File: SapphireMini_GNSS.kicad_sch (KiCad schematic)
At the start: 7 parts, among them J401 Conn_01x01_Male, J402 Conn_01x04_Male, U402 SAM-M8Q-0-10

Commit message: Start of layout
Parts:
- added R402, R403: 0, Resistor_SMD:R_0603_1608Metric, symbol Device:R_Small_US
- C401: footprint Capacitor_SMD:C_0603_1608Metric -> Capacitor_SMD:C_0402_1005Metric
- R401: MPN (none) -> EXB-2HV470JV
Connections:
- net SAM_SCL: now also R402.2; no longer U402.12 (SCL)
- net SAM_SDA: now also R403.2; no longer U402.9 (SDA)
- new net: R402.1, U402.12 (SCL)
- new net: R403.1, U402.9 (SDA)
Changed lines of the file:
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@@
     (comment 2 "Markup copy w/ errors!")
   )
-  (junction (at 64.77 46.99) (diameter 0) (color 0 0 0 0)
-  )
   (junction (at 95.25 90.17) (diameter 0) (color 0 0 0 0)
   )
   (junction (at 95.25 46.99) (diameter 0) (color 0 0 0 0)
   )
-  (junction (at 134.62 92.71) (diameter 0) (color 0 0 0 0)
-  )
   (junction (at 95.25 95.25) (diameter 0) (color 0 0 0 0)
   )
@@
     (stroke (width 0) (type default) (color 0 0 0 0))
   )
+  (wire (pts (xy 115.57 107.95) (xy 135.89 107.95))
+    (stroke (width 0) (type default) (color 0 0 0 0))
+  )
   (wire (pts (xy 110.49 55.88) (xy 111.76 54.61))
     (stroke (width 0) (type default) (color 0 0 0 0))
@@
     (stroke (width 0) (type default) (color 0 0 0 0))
   )
-  (wire (pts (xy 95.25 46.99) (xy 64.77 46.99))
+  (wire (pts (xy 55.88 46.99) (xy 95.25 46.99))
+    (stroke (width 0) (type default) (color 0 0 0 0))
+  )
+  (wire (pts (xy 115.57 105.41) (xy 135.89 105.41))
     (stroke (width 0) (type default) (color 0 0 0 0))
   )
@@
     (stroke (width 0) (type default) (color 0 0 0 0))
   )
-  (wire (pts (xy 115.57 105.41) (xy 135.89 105.41))
-    (stroke (width 0) (type default) (color 0 0 0 0))
-  )
   (wire (pts (xy 176.53 100.33) (xy 187.96 100.33))
     (stroke (width 0) (type default) (color 0 0 0 0))
@@
     (stroke (width 0) (type default) (color 0 0 0 0))
   )
-  (wire (pts (xy 115.57 92.71) (xy 134.62 92.71))
+  (wire (pts (xy 115.57 92.71) (xy 135.89 92.71))
     (stroke (width 0) (type default) (color 0 0 0 0))
   )
@@
     (stroke (width 0) (type default) (color 0 0 0 0))
   )
-  (wire (pts (xy 134.62 92.71) (xy 135.89 92.71))
-    (stroke (width 0) (type default) (color 0 0 0 0))
-  )
   (wire (pts (xy 40.64 85.09) (xy 52.07 85.09))
     (stroke (width 0) (type default) (color 0 0 0 0))
@@
     (stroke (width 0) (type default) (color 0 0 0 0))
   )
-  (wire (pts (xy 64.77 46.99) (xy 55.88 46.99))
-    (stroke (width 0) (type default) (color 0 0 0 0))
-  )
   (wire (pts (xy 115.57 100.33) (xy 135.89 100.33))
     (stroke (width 0) (type default) (color 0 0 0 0))
   )
+  (wire (pts (xy 182.88 105.41) (xy 194.31 105.41))
+    (stroke (width 0) (type default) (color 0 0 0 0))
+  )
   (wire (pts (xy 95.25 46.99) (xy 95.25 90.17))
     (stroke (width 0) (type default) (color 0 0 0 0))
@@
     (stroke (width 0) (type default) (color 0 0 0 0))
   )
-  (wire (pts (xy 115.57 107.95) (xy 135.89 107.95))
-    (stroke (width 0) (type default) (color 0 0 0 0))
-  )
   (wire (pts (xy 130.81 124.46) (xy 130.81 116.84))
     (stroke (width 0) (type default) (color 0 0 0 0))
@@
     (stroke (width 0) (type default) (color 0 0 0 0))
   )
-  (wire (pts (xy 176.53 105.41) (xy 187.96 105.41))
+  (wire (pts (xy 176.53 105.41) (xy 177.8 105.41))
     (stroke (width 0) (type default) (color 0 0 0 0))
   )
@@
     (stroke (width 0) (type default) (color 0 0 0 0))
   )
-  (wire (pts (xy 176.53 107.95) (xy 187.96 107.95))
+  (wire (pts (xy 182.88 107.95) (xy 194.31 107.95))
+    (stroke (width 0) (type default) (color 0 0 0 0))
+  )
+  (wire (pts (xy 176.53 107.95) (xy 177.8 107.95))
     (stroke (width 0) (type default) (color 0 0 0 0))
   )
@@
     (effects (font (size 1.27 1.27)) (justify left bottom))
   )
-  (label "SAM_SDA" (at 177.8 107.95 0)
-    (effects (font (size 1.27 1.27)) (justify left bottom))
-  )
-  (label "V_BCKP" (at 120.65 92.71 0)
+  (label "SAM_SDA" (at 185.42 107.95 0)
     (effects (font (size 1.27 1.27)) (justify left bottom))
   )
@@
     (effects (font (size 1.27 1.27)) (justify left bottom))
   )
-  (label "SAM_SCL" (at 177.8 105.41 0)
+  (label "SAM_SCL" (at 185.42 105.41 0)
     (effects (font (size 1.27 1.27)) (justify left bottom))
   )
@@
   )
   (label "SAM_SCL" (at 68.58 95.25 0)
+    (effects (font (size 1.27 1.27)) (justify left bottom))
+  )
+  (label "V_BCKP" (at 124.46 92.71 0)
     (effects (font (size 1.27 1.27)) (justify left bottom))
   )
@@
       (effects (font (size 1.27 1.27)) (justify left))
     )
-    (property "Footprint" "Capacitor_SMD:C_0603_1608Metric" (id 2) (at 95.25 101.6 0)
+    (property "Footprint" "Capacitor_SMD:C_0402_1005Metric" (id 2) (at 95.25 101.6 0)
       (effects (font (size 1.27 1.27)) hide)
     )
@@
     (pin "1")
   )
-  (symbol (lib_id "power:PWR_FLAG") (at 64.77 46.99 0) (unit 1)
-    (in_bom yes) (on_board yes) (fields_autoplaced)
-    (property "Reference" "#FLG0401" (id 0) (at 64.77 45.085 0)
-      (effects (font (size 1.27 1.27)) hide)
-    )
-    (property "Value" "PWR_FLAG" (id 1) (at 64.77 43.4142 0))
-    (property "Footprint" "" (id 2) (at 64.77 46.99 0)
-      (effects (font (size 1.27 1.27)) hide)
-    )
-    (property "Datasheet" "~" (id 3) (at 64.77 46.99 0)
-      (effects (font (size 1.27 1.27)) hide)
-    )
-    (pin "1")
+  (symbol (lib_id "Device:R_Small_US") (at 180.34 105.41 90) (unit 1)
+    (in_bom yes) (on_board yes)
+    (property "Reference" "R402" (id 0) (at 177.8 102.87 90)
+      (effects (font (size 1.27 1.27)) (justify right))
+    )
+    (property "Value" "0" (id 1) (at 180.34 102.87 90)
+      (effects (font (size 1.27 1.27)) (justify right))
+    )
+    (property "Footprint" "Resistor_SMD:R_0603_1608Metric" (id 2) (at 180.34 105.41 0)
+      (effects (font (size 1.27 1.27)) hide)
+    )
+    (property "Datasheet" "~" (id 3) (at 180.34 105.41 0)
+      (effects (font (size 1.27 1.27)) hide)
+    )
+    (property "MPN" "RMCF0603ZT0R00" (id 4) (at 180.34 105.41 0)
+      (effects (font (size 1.27 1.27)) hide)
+    )
+    (property "Manufacturer" "Vishay" (id 5) (at 180.34 105.41 0)
+      (effects (font (size 1.27 1.27)) hide)
+    )
+    (property "DPN" "WSLJ-.1CT-ND" (id 6) (at 180.34 105.41 0)
+      (effects (font (size 1.27 1.27)) hide)
+    )
+    (property "Populate" "1" (id 7) (at 180.34 105.41 0)
+      (effects (font (size 1.27 1.27)) hide)
+    )
+    (property "Description" "0 Ohms Jumper 0.1W, 1/10W Chip Resistor 0603 (1608 Metric) Automotive AEC-Q200 Thick Film" (id 8) (at 180.34 105.41 0)
+      (effects (font (size 1.27 1.27)) hide)
+    )
+    (property "Digi-Key_PN" "WSLJ-.1CT-ND" (id 9) (at 180.34 105.41 0)
+      (effects (font (size 1.27 1.27)) hide)
+    )
+    (property "Distributor" "Digikey" (id 10) (at 180.34 105.41 0)
+      (effects (font (size 1.27 1.27)) hide)
+    )
+    (pin "1")
+    (pin "2")
   )
   (symbol (lib_id "Device:FerriteBead") (at 46.99 105.41 90) (unit 1)
@@
     (pin "4")
   )
+  (symbol (lib_id "Device:R_Small_US") (at 180.34 107.95 90) (unit 1)
+    (in_bom yes) (on_board yes)
+    (property "Reference" "R403" (id 0) (at 177.8 110.49 90)
+      (effects (font (size 1.27 1.27)) (justify right))
+    )
+    (property "Value" "0" (id 1) (at 180.34 110.49 90)
+      (effects (font (size 1.27 1.27)) (justify right))
+    )
+    (property "Footprint" "Resistor_SMD:R_0603_1608Metric" (id 2) (at 180.34 107.95 0)
+      (effects (font (size 1.27 1.27)) hide)
+    )
+    (property "Datasheet" "~" (id 3) (at 180.34 107.95 0)
+      (effects (font (size 1.27 1.27)) hide)
+    )
+    (property "MPN" "RMCF0603ZT0R00" (id 4) (at 180.34 107.95 0)
+      (effects (font (size 1.27 1.27)) hide)
+    )
+    (property "Manufacturer" "Vishay" (id 5) (at 180.34 107.95 0)
+      (effects (font (size 1.27 1.27)) hide)
+    )
+    (property "DPN" "WSLJ-.1CT-ND" (id 6) (at 180.34 107.95 0)
+      (effects (font (size 1.27 1.27)) hide)
+    )
+    (property "Populate" "1" (id 7) (at 180.34 107.95 0)
+      (effects (font (size 1.27 1.27)) hide)
+    )
+    (property "Description" "0 Ohms Jumper 0.1W, 1/10W Chip Resistor 0603 (1608 Metric) Automotive AEC-Q200 Thick Film" (id 8) (at 180.34 107.95 0)
+      (effects (font (size 1.27 1.27)) hide)
+    )
+    (property "Digi-Key_PN" "WSLJ-.1CT-ND" (id 9) (at 180.34 107.95 0)
+      (effects (font (size 1.27 1.27)) hide)
+    )
+    (property "Distributor" "Digikey" (id 10) (at 180.34 107.95 0)
+      (effects (font (size 1.27 1.27)) hide)
+    )
+    (pin "1")
+    (pin "2")
+  )
   (symbol (lib_id "power:GND") (at 95.25 124.46 0) (unit 1)
     (in_bom yes) (on_board yes)
@@
     (property "Datasheet" "" (id 3) (at 52.07 80.01 0)
       (effects (font (size 1.524 1.524)))
+    )
+    (property "MPN" "EXB-2HV470JV" (id 4) (at 52.07 80.01 0)
+      (effects (font (size 1.27 1.27)) hide)
     )
     (pin "1")
@@
     (pin "2")
   )
-  (symbol (lib_id "power:PWR_FLAG") (at 134.62 92.71 0) (unit 1)
-    (in_bom yes) (on_board yes) (fields_autoplaced)
-    (property "Reference" "#FLG0402" (id 0) (at 134.62 90.805 0)
-      (effects (font (size 1.27 1.27)) hide)
-    )
-    (property "Value" "PWR_FLAG" (id 1) (at 134.62 89.1342 0))
-    (property "Footprint" "" (id 2) (at 134.62 92.71 0)
-      (effects (font (size 1.27 1.27)) hide)
-    )
-    (property "Datasheet" "~" (id 3) (at 134.62 92.71 0)
-      (effects (font (size 1.27 1.27)) hide)
-    )
-    (pin "1")
-  )
   (symbol (lib_id "power:GND") (at 110.49 60.96 0) (unit 1)

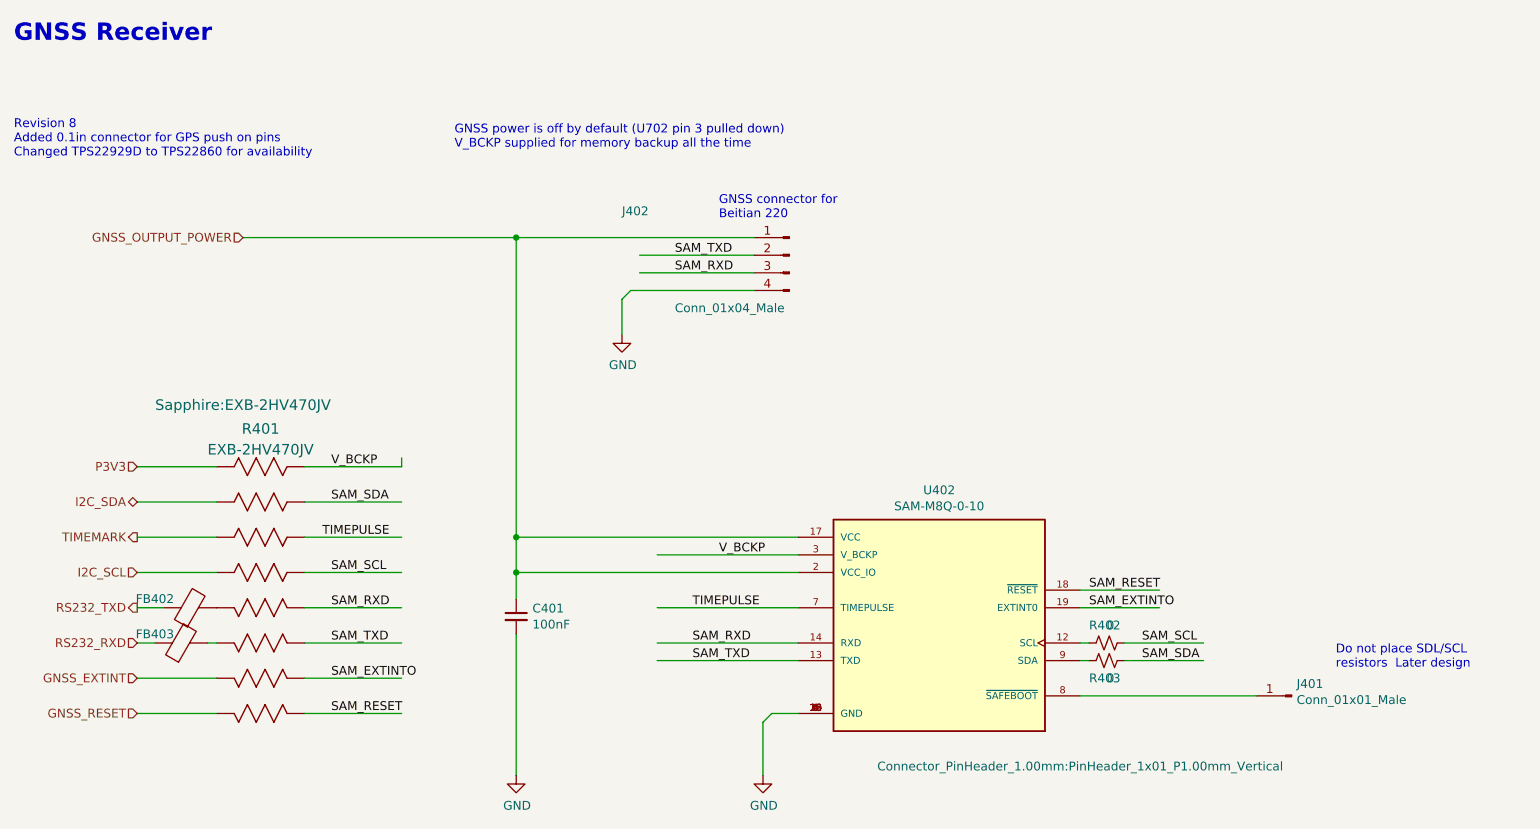
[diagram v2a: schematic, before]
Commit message: updated new layout - no routing
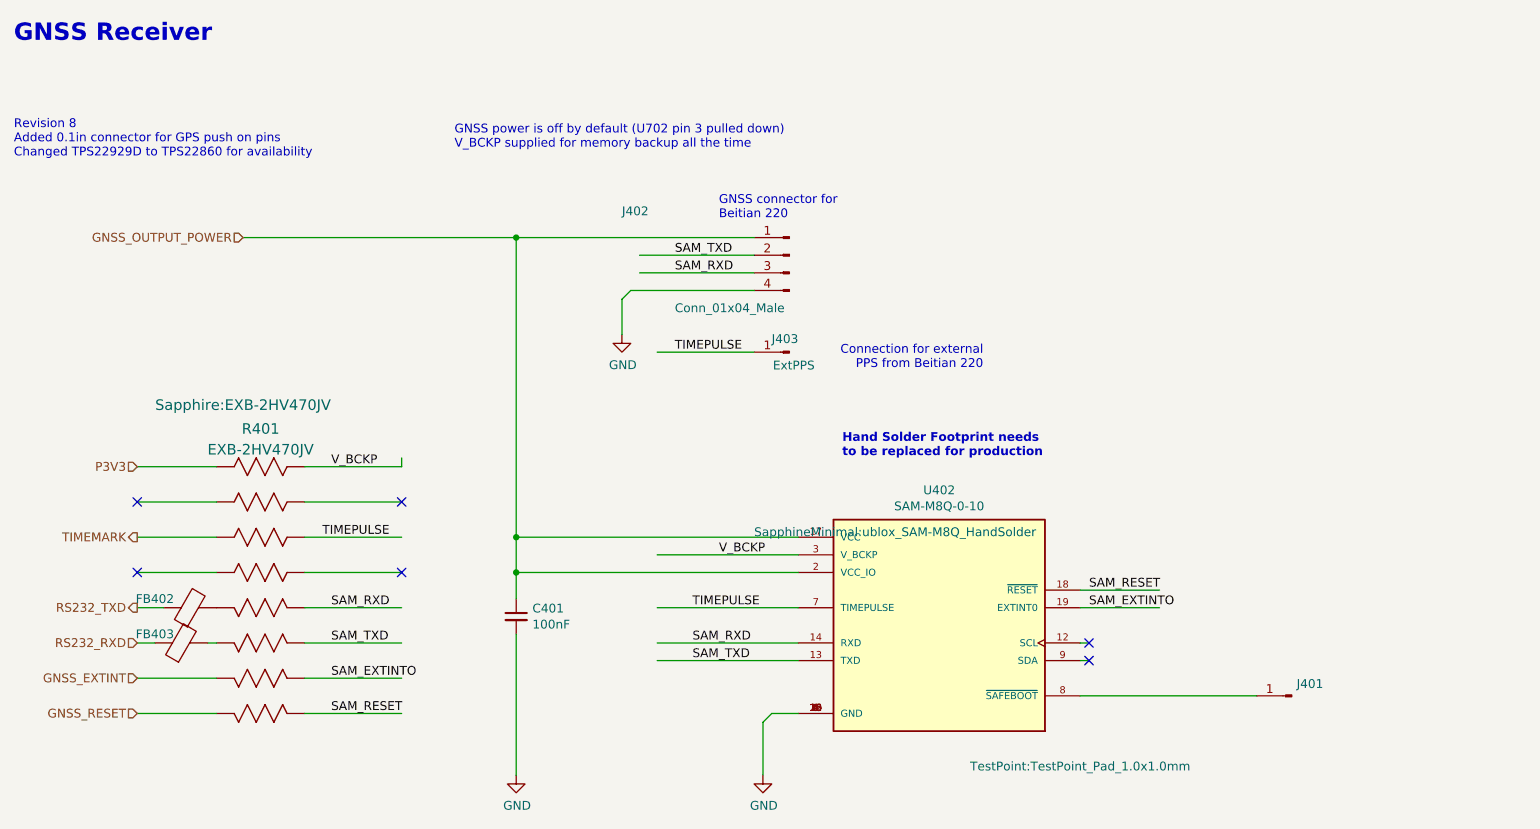
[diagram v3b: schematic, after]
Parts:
- removed R402, R403: 0, Resistor_SMD:R_0603_1608Metric, symbol Device:R_Small_US
- added J403: ExtPPS, TestPoint:TestPoint_Pad_1.5x1.5mm, symbol Connector:Conn_01x01_Male
- J401: footprint Connector_PinHeader_1.00mm:PinHeader_1x01_P1.00mm_Vertical -> TestPoint:TestPoint_Pad_1.0x1.0mm
- R401: symbol PanasonicRA:EXB-2HV470JV -> sapphireMini:EXB-2HV470JV_1
- U402: footprint SapphineMinimal:MODULE_SAM-M8Q-0-10 -> SapphineMinimal:ublox_SAM-M8Q_HandSolder
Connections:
- net TIMEPULSE: now also J403.1 (Pin_1)
- net I2C_SCL: no longer names the net of R401.4
- net I2C_SDA: no longer names the net of R401.2
- net SAM_SCL: no longer names the net of R401.13
- net SAM_SDA: no longer names the net of R401.15
- no-connect marks 0 -> 6
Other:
- note added: "Connection for external PPS from Beitian 220"
- note added: "Hand Solder Footprint needs to be replaced for production"
- note removed: "Do not place SDL/SCL resistors Later design"

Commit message: 6 Layer Routing
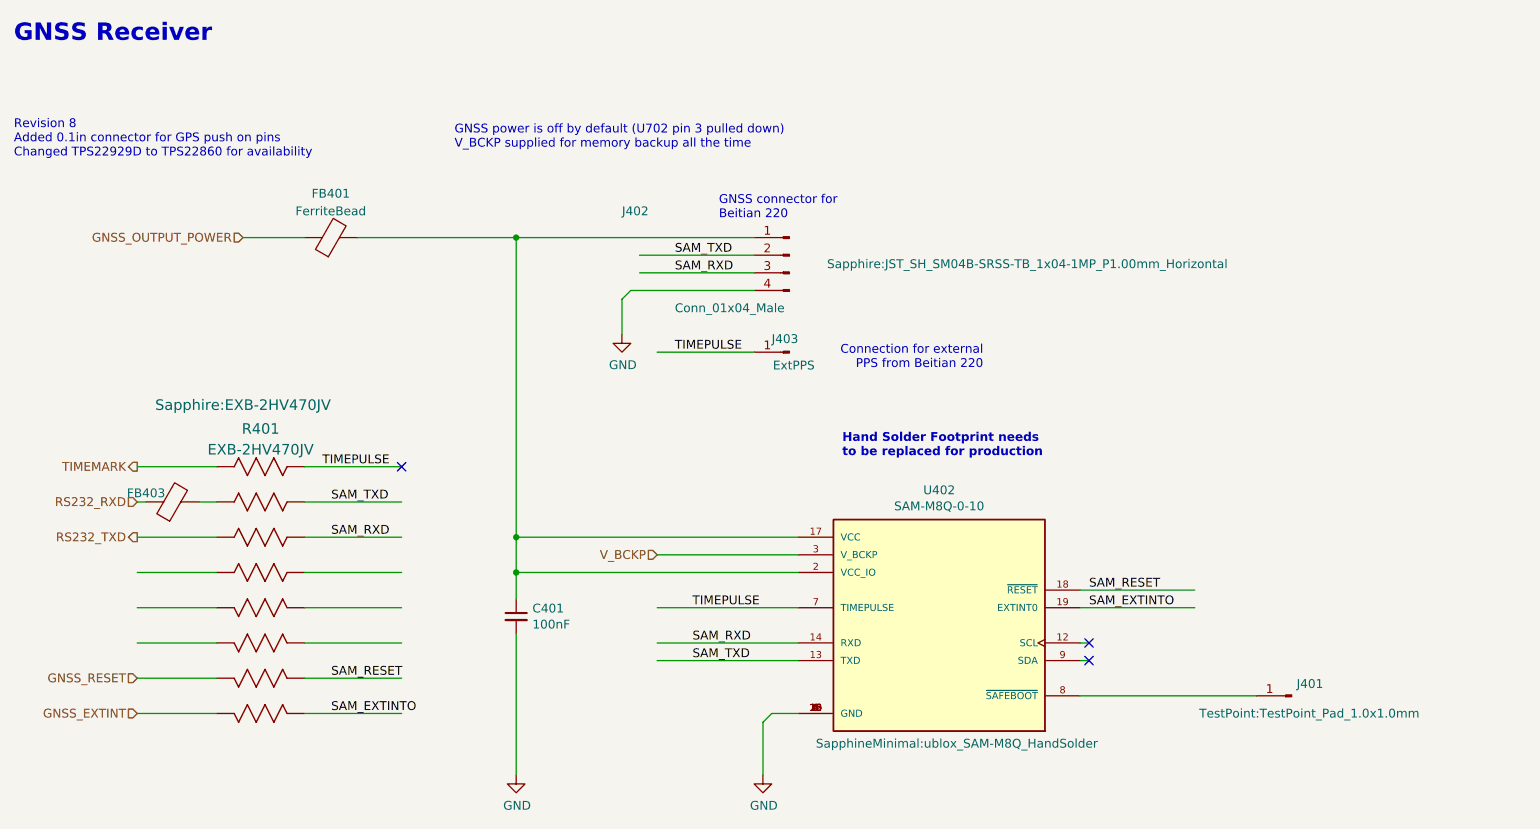
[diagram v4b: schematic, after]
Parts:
- removed FB402: FerriteBead, Inductor_SMD:L_0201_0603Metric, symbol Device:FerriteBead
- added FB401: FerriteBead, Inductor_SMD:L_0603_1608Metric, symbol Device:FerriteBead
- FB403: footprint Inductor_SMD:L_0201_0603Metric -> Inductor_SMD:L_0603_1608Metric
- J402: footprint Connector_JST:JST_SH_SM04B-SRSS-TB_1x04-1MP_P1.00mm_Horizontal -> Sapphire:JST_SH_SM04B-SRSS-TB_1x04-1MP_P1.00mm_Horizontal; symbol Connector:Conn_01x04_Male -> sapphireMini:Conn_01x04_Male
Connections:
- net P3V3 is gone; now on net TIMEMARK: R401.1
- net GNSS_EXTINT: now also R401.8; no longer R401.7
- net GNSS_OUTPUT_POWER: now also FB401.1; no longer C401.1, J402.1 (Pin_1), U402.17 (VCC), U402.2 (VCC_IO)
- net GNSS_RESET: now also R401.7; no longer R401.8
- net RS232_TXD: now also R401.3
- net SAM_EXTINTO: now also R401.9; no longer R401.10
- net SAM_RESET: now also R401.10; no longer R401.9
- net SAM_RXD: now also R401.14; no longer R401.12
- net SAM_TXD: now also R401.15; no longer R401.11
- net TIMEMARK: no longer R401.3
- net TIMEPULSE: now also R401.16; no longer R401.14
- net V_BCKP: no longer R401.16
- net at FB403.2: now also R401.2; no longer R401.6
- new net: C401.1, FB401.2, J402.1 (Pin_1), U402.17 (VCC), U402.2 (VCC_IO)
- no-connect marks 6 -> 3
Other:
- moved on the sheet: FB403

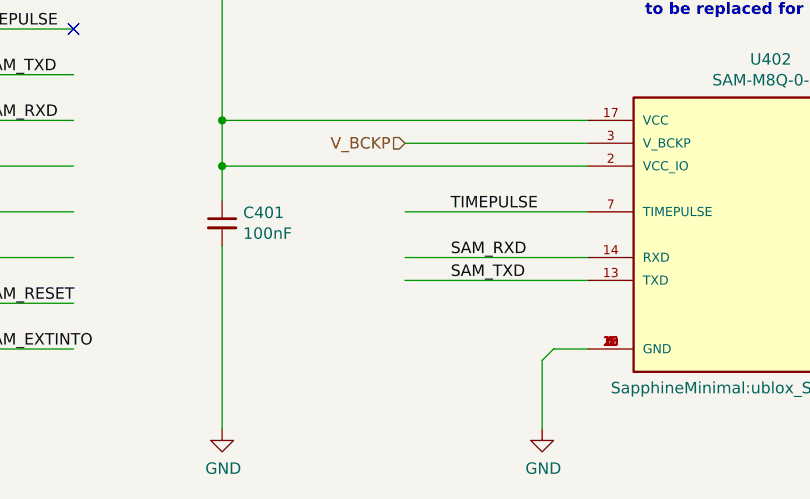
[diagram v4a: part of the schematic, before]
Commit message: Updated to fix noted problems
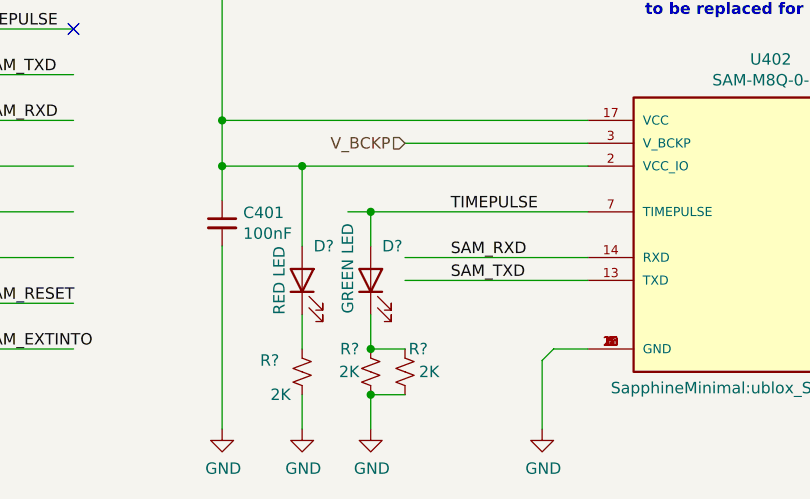
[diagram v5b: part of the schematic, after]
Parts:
- added D?: RED LED, LED_SMD:LED_0805_2012Metric, symbol Device:LED
- added D?: GREEN LED, LED_SMD:LED_0805_2012Metric, symbol Device:LED
- added R? (x3): 2K, Resistor_SMD:R_0603_1608Metric, symbol Device:R_Small_US
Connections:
- net GND: now also R?.1, R?.1, R?.1
- net TIMEPULSE: now also D?.2 (A)
- net at C401.1, FB401.2, J402.1 (Pin_1)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: now also D?.2 (A)
- new net: D?.1 (K), R?.2, R?.2
- new net: D?.1 (K), R?.2
